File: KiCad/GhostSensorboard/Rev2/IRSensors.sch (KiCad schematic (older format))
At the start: 24 parts, among them U1 TCA9548ARGER, U10 GP2Y0E02B, U11 GP2Y0E02B, U12 GP2Y0E02B, U13 GP2Y0E02B, U14 GP2Y0E02B, U15 GP2Y0E02B, U16 GP2Y0E02B, U17 GP2Y0E02B, U18 GP2Y0E02B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

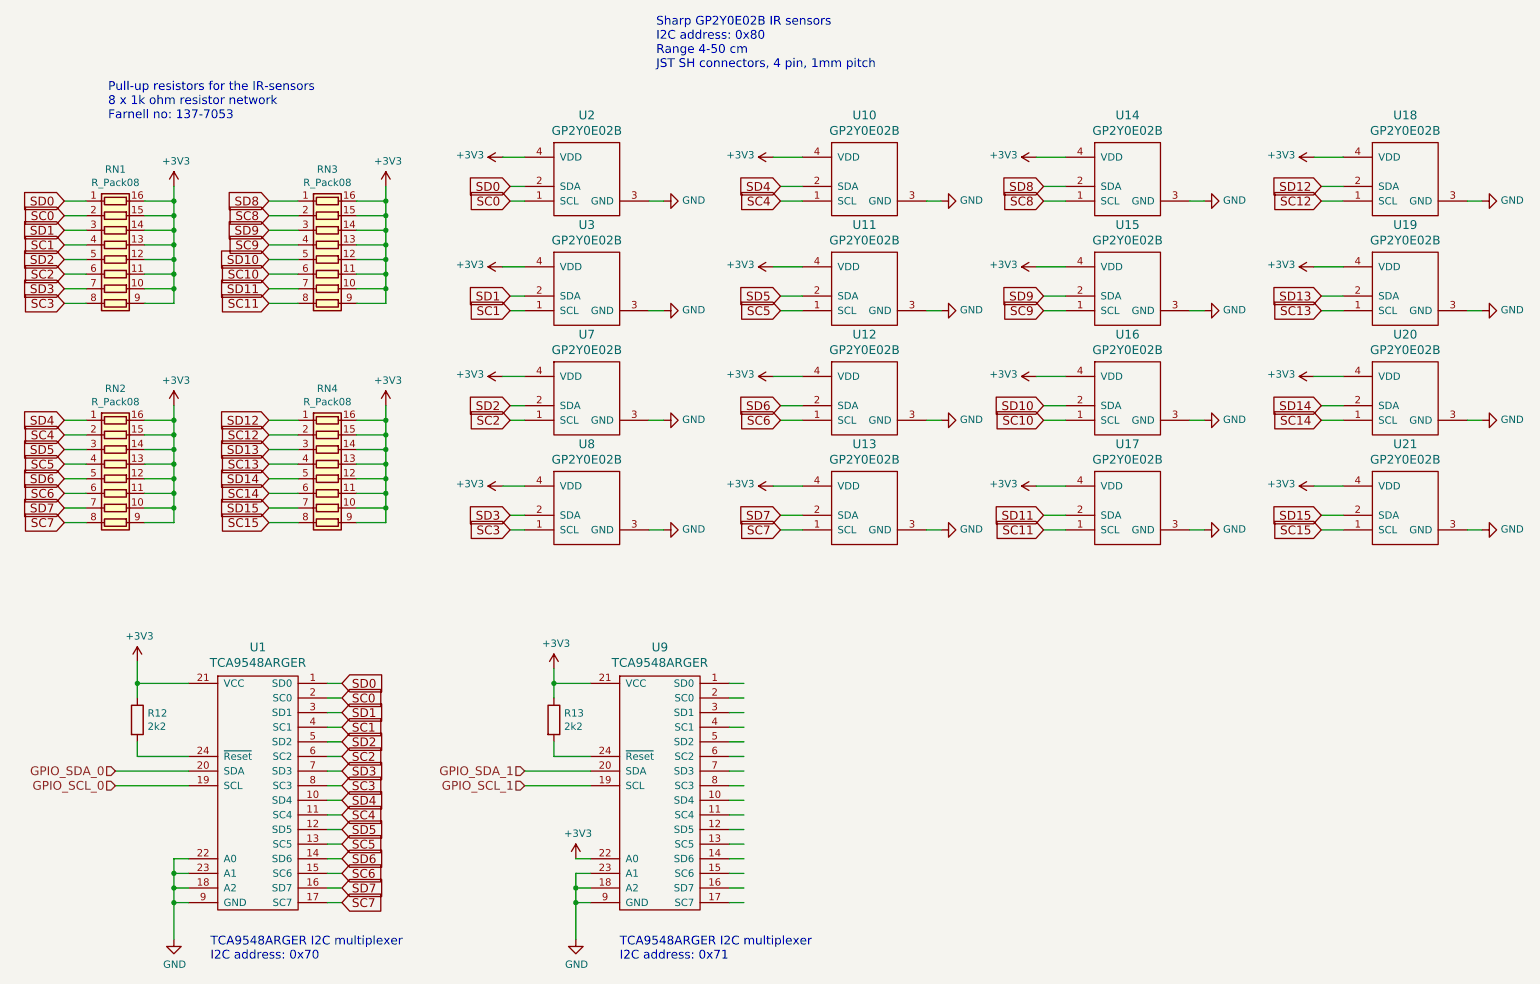
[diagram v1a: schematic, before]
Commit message: Ready to start routing. Schematics should be done.
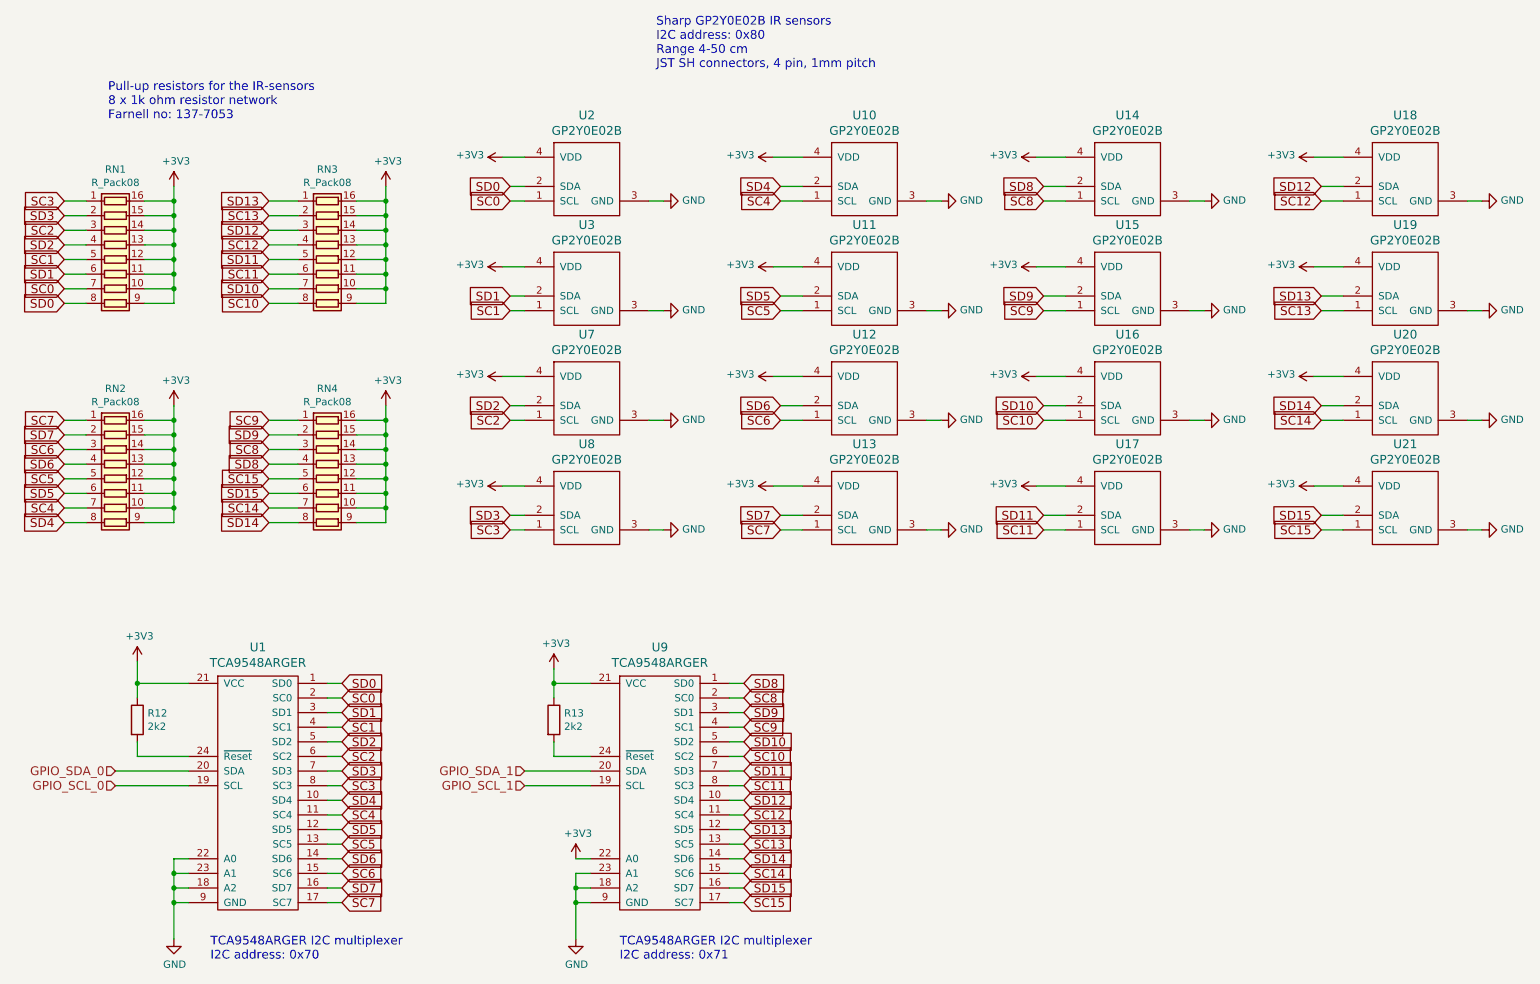
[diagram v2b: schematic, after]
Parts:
- R12, R13: footprint Resistors_SMD:R_0603 -> Resistors_SMD:R_0402

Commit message: Rev2 sent to Elecrow for production
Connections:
- net SC10: now also RN3.7 (R7.1); no longer RN3.8 (R8.1)
- net SC11: now also RN3.5 (R5.1); no longer RN3.6 (R6.1)
- net SC12: now also RN3.3 (R3.1); no longer RN3.4 (R4.1)
- net SC13: now also RN3.1 (R1.1); no longer RN3.2 (R2.1)
- net SD10: now also RN3.8 (R8.1); no longer RN3.7 (R7.1)
- net SD11: now also RN3.6 (R6.1); no longer RN3.5 (R5.1)
- net SD12: now also RN3.4 (R4.1); no longer RN3.3 (R3.1)
- net SD13: now also RN3.2 (R2.1); no longer RN3.1 (R1.1)
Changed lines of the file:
@@
 Sheet 2 2
 Title "Ghost Sensorboard"
-Date "2017-03-19"
+Date "2017-03-20"
 Rev "2"
 Comp "Frode Lillerud"
-Comment1 "Work in progress"
+Comment1 "https://github.com/Scalpel78/Ghost/tree/master/KiCad/GhostSensorboard/Rev2"
 Comment2 ""
 Comment3 ""
@@
 Text GLabel 2550 3700 0    60   Input ~ 0
 SC9
+Text GLabel 2550 2900 0    60   Input ~ 0
+SD10
 Text GLabel 2550 2800 0    60   Input ~ 0
-SD10
-Text GLabel 2550 2900 0    60   Input ~ 0
 SC10
+Text GLabel 2550 2700 0    60   Input ~ 0
+SD11
 Text GLabel 2550 2600 0    60   Input ~ 0
-SD11
-Text GLabel 2550 2700 0    60   Input ~ 0
 SC11
+Text GLabel 2550 2500 0    60   Input ~ 0
+SD12
 Text GLabel 2550 2400 0    60   Input ~ 0
-SD12
-Text GLabel 2550 2500 0    60   Input ~ 0
 SC12
+Text GLabel 2550 2300 0    60   Input ~ 0
+SD13
 Text GLabel 2550 2200 0    60   Input ~ 0
-SD13
-Text GLabel 2550 2300 0    60   Input ~ 0
 SC13
 Text GLabel 2550 4400 0    60   Input ~ 0
